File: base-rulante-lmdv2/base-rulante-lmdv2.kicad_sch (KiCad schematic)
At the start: 27 parts, among them J1 RJ_can, J2 RJ_can, J5 connector_power, U1 Nucleo_STM32G431KB, U2 LMD18200, U2 MCP2551-I-SN, U3 LMD18200

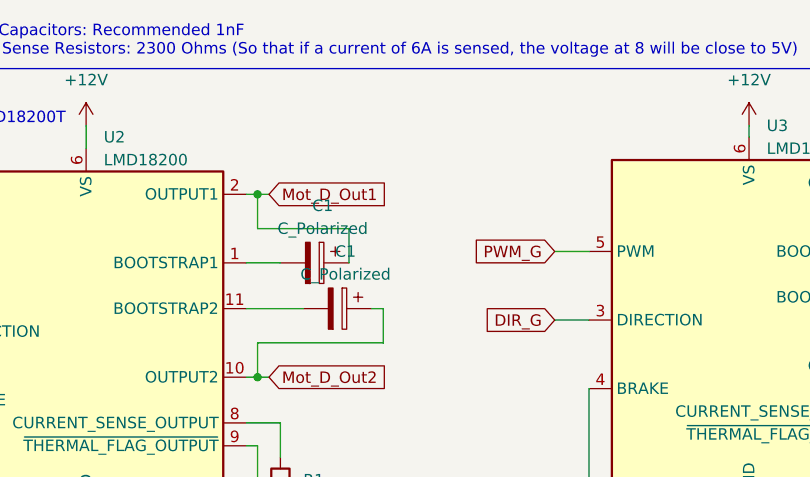
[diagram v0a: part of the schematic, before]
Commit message: base roulante reroute au cas ou
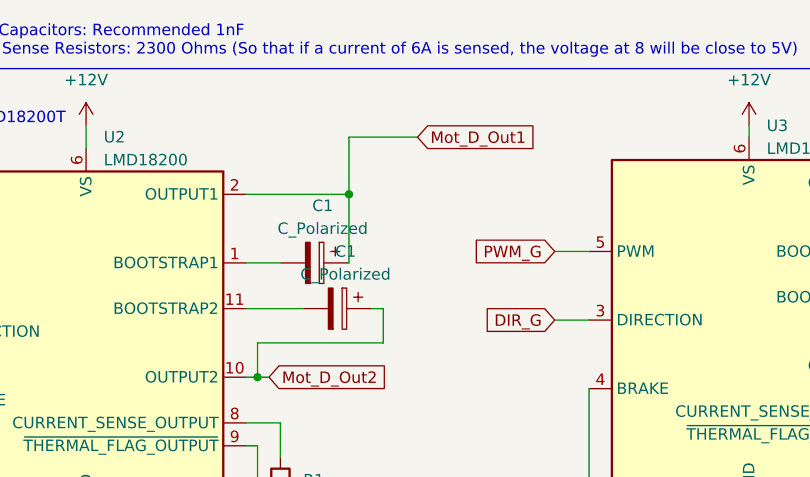
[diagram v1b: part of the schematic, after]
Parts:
- C1: footprint Capacitor_THT:CP_Radial_D5.0mm_P2.00mm -> Capacitor_SMD:C_0805_2012Metric
